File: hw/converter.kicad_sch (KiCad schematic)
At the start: 16 parts, among them J301 1935776, J302 1935776, Q301 SW_L, Q302 SW_H

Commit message: hw changes
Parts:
- HS301: footprint mppt:WayinTop_HS -> footprints:WayinTop_HS
- J301, J302: footprint mppt:1935776 -> footprints:1935776
- L301: footprint mppt:B65878E1012D001 -> footprints:B65878E1012D001
- Q301, Q302: footprint mppt:EPC2307 -> footprints:EPC2307
- TP302, TP410: footprint mppt:SignalTP -> footprints:SignalTP
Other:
- moved on the sheet: C304
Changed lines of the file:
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@@
   (junction (at 134.62 71.12) (diameter 0) (color 0 0 0 0)
   )
-  (junction (at 198.755 71.12) (diameter 0) (color 0 0 0 0)
+  (junction (at 198.12 71.12) (diameter 0) (color 0 0 0 0)
   )
   (junction (at 157.48 85.09) (diameter 0) (color 0 0 0 0)
@@
   (junction (at 180.34 109.22) (diameter 0) (color 0 0 0 0)
   )
-  (junction (at 198.755 109.22) (diameter 0) (color 0 0 0 0)
+  (junction (at 198.12 109.22) (diameter 0) (color 0 0 0 0)
   )
   (junction (at 156.21 109.22) (diameter 0) (color 0 0 0 0)
@@
     (stroke (width 0) (type default))
   )
-  (wire (pts (xy 180.34 71.12) (xy 198.755 71.12))
+  (wire (pts (xy 180.34 71.12) (xy 198.12 71.12))
     (stroke (width 0) (type default))
   )
@@
     (stroke (width 0) (type default))
   )
-  (wire (pts (xy 198.755 93.98) (xy 198.755 109.22))
+  (wire (pts (xy 198.12 93.98) (xy 198.12 109.22))
     (stroke (width 0) (type default))
   )
@@
     (stroke (width 0) (type default))
   )
-  (wire (pts (xy 198.755 71.12) (xy 214.63 71.12))
+  (wire (pts (xy 198.12 71.12) (xy 214.63 71.12))
     (stroke (width 0) (type default))
   )
@@
     (stroke (width 0) (type default))
   )
-  (wire (pts (xy 180.34 109.22) (xy 198.755 109.22))
+  (wire (pts (xy 180.34 109.22) (xy 198.12 109.22))
     (stroke (width 0) (type default))
   )
@@
     (stroke (width 0) (type default))
   )
-  (wire (pts (xy 198.755 71.12) (xy 198.755 86.36))
+  (wire (pts (xy 198.12 71.12) (xy 198.12 86.36))
     (stroke (width 0) (type default))
   )
@@
     (stroke (width 0) (type default))
   )
-  (wire (pts (xy 198.755 109.22) (xy 214.63 109.22))
+  (wire (pts (xy 198.12 109.22) (xy 214.63 109.22))
     (stroke (width 0) (type default))
   )
@@
       (effects (font (size 1 1)))
     )
-    (property "Footprint" "mppt:1935776" (at 40.64 88.9 0)
+    (property "Footprint" "footprints:1935776" (at 40.64 88.9 0)
       (effects (font (size 1.27 1.27)) (justify bottom) hide)
     )
@@
       (effects (font (size 1 1)) (justify left))
     )
-    (property "Footprint" "mppt:EPC2307" (at 160.02 87.63 0)
+    (property "Footprint" "footprints:EPC2307" (at 160.02 87.63 0)
       (effects (font (size 1.27 1.27)) hide)
     )
@@
       (effects (font (size 1 1)))
     )
-    (property "Footprint" "mppt:1935776" (at 256.54 88.9 0)
+    (property "Footprint" "footprints:1935776" (at 256.54 88.9 0)
       (effects (font (size 1.27 1.27)) (justify bottom) hide)
     )
@@
       (effects (font (size 1 1)))
     )
-    (property "Footprint" "mppt:EPC2307" (at 167.64 73.66 0)
+    (property "Footprint" "footprints:EPC2307" (at 167.64 73.66 0)
       (effects (font (size 1.27 1.27)) hide)
     )
@@
       (effects (font (size 1 1)) (justify left))
     )
-    (property "Footprint" "mppt:SignalTP" (at 114.3 97.79 0)
+    (property "Footprint" "footprints:SignalTP" (at 114.3 97.79 0)
       (effects (font (size 1.27 1.27)) hide)
     )
@@
       (effects (font (size 1 1)) (justify left))
     )
-    (property "Footprint" "mppt:SignalTP" (at 165.1 90.17 0)
+    (property "Footprint" "footprints:SignalTP" (at 165.1 90.17 0)
       (effects (font (size 1.27 1.27)) hide)
     )
@@
       (effects (font (size 1 1)) (justify left))
     )
-    (property "Footprint" "mppt:WayinTop_HS" (at 159.0548 55.88 0)
+    (property "Footprint" "footprints:WayinTop_HS" (at 159.0548 55.88 0)
       (effects (font (size 1.27 1.27)) hide)
     )
@@
     )
   )
-  (symbol (lib_id "Device:C") (at 198.755 90.17 0) (unit 1)
-    (in_bom yes) (on_board yes) (dnp no)
-    (property "Reference" "C304" (at 202.565 88.8999 0)
-      (effects (font (size 1 1)) (justify left))
-    )
-    (property "Value" "18uF" (at 202.565 91.4399 0)
-      (effects (font (size 1 1)) (justify left))
-    )
-    (property "Footprint" "Capacitor_THT:C_Radial_D10.0mm_H16.0mm_P5.00mm" (at 199.7202 93.98 0)
-      (effects (font (size 1.27 1.27)) hide)
-    )
-    (property "Datasheet" "https://www.mouser.com/datasheet/2/212/KEM_A4072_A759-1104329.pdf" (at 198.755 90.17 0)
-      (effects (font (size 1.27 1.27)) hide)
-    )
-    (property "Distributor" "Mouser" (at 198.755 90.17 0)
-      (effects (font (size 1.27 1.27)) hide)
-    )
-    (property "Manufacturer" "KEMET" (at 198.755 90.17 0)
-      (effects (font (size 1.27 1.27)) hide)
-    )
-    (property "P/N" "80-A759MS186M2CAAE90" (at 198.755 90.17 0)
-      (effects (font (size 1.27 1.27)) hide)
-    )
-    (property "LCSC Part #" "" (at 198.755 90.17 0)
-      (effects (font (size 1.27 1.27)) hide)
-    )
-    (property "Cost" "2.58" (at 198.755 90.17 0)
+  (symbol (lib_id "Device:C") (at 198.12 90.17 0) (unit 1)
+    (in_bom yes) (on_board yes) (dnp no)
+    (property "Reference" "C304" (at 201.93 88.8999 0)
+      (effects (font (size 1 1)) (justify left))
+    )
+    (property "Value" "18uF" (at 201.93 91.4399 0)
+      (effects (font (size 1 1)) (justify left))
+    )
+    (property "Footprint" "Capacitor_THT:C_Radial_D10.0mm_H16.0mm_P5.00mm" (at 199.0852 93.98 0)
+      (effects (font (size 1.27 1.27)) hide)
+    )
+    (property "Datasheet" "https://www.mouser.com/datasheet/2/212/KEM_A4072_A759-1104329.pdf" (at 198.12 90.17 0)
+      (effects (font (size 1.27 1.27)) hide)
+    )
+    (property "Distributor" "Mouser" (at 198.12 90.17 0)
+      (effects (font (size 1.27 1.27)) hide)
+    )
+    (property "Manufacturer" "KEMET" (at 198.12 90.17 0)
+      (effects (font (size 1.27 1.27)) hide)
+    )
+    (property "P/N" "80-A759MS186M2CAAE90" (at 198.12 90.17 0)
+      (effects (font (size 1.27 1.27)) hide)
+    )
+    (property "LCSC Part #" "" (at 198.12 90.17 0)
+      (effects (font (size 1.27 1.27)) hide)
+    )
+    (property "Cost" "2.58" (at 198.12 90.17 0)
       (effects (font (size 1.27 1.27)) hide)
     )
@@
       (effects (font (size 1 1)))
     )
-    (property "Footprint" "mppt:B65878E1012D001" (at 101.6 50.8 0)
+    (property "Footprint" "footprints:B65878E1012D001" (at 101.6 50.8 0)
       (effects (font (size 1.27 1.27)) (justify left) hide)
     )

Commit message: v0.2.0
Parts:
- removed C302: CP, TestPoint:TestPoint_2Pads_Pitch2.54mm_Drill0.8mm, symbol Device:C
- removed D301: Schottky, TestPoint:TestPoint_2Pads_Pitch2.54mm_Drill0.8mm, symbol Device:D_Schottky
- removed D302: D_TVS, Diode_SMD:D_SMC, symbol Device:D_TVS
- removed HS301: Heatsink_Pad, footprints:WayinTop_HS, symbol Mechanical:Heatsink
- removed J301, J302: 1935776, footprints:1935776, symbol 1935776:1935776
- removed L301: B65878E1012D001, footprints:B65878E1012D001, symbol B65878E1012D001:B65878E1012D001
- removed R301: R, TestPoint:TestPoint_2Pads_Pitch2.54mm_Drill0.8mm, symbol Device:R
- removed TP410: TestPoint_2Pole, footprints:SignalTP, symbol Connector:TestPoint_2Pole
- added C301: 2.2uF, Capacitor_SMD:C_2220_5650Metric, symbol Device:C
- added F301, F302: Fuse_Small, footprints:littelfuse_05200101Z, symbol Device:Fuse
- added J301, J302: XT60PW-M, Connector_AMASS:AMASS_XT60PW-M_1x02_P7.20mm_Horizontal, symbol amass_XT60PW_M:XT60PW-M
- added L301: B65878E1012D001, footprints:tdk_B65878E1012D001, symbol tdk_B65878E1012D001:B65878E1012D001
- Q301, Q302: footprint footprints:EPC2307 -> footprints:epc_EPC2307
- TP301: renamed from TP302; value TestPoint_2Pole -> VSW_TP; footprint footprints:SignalTP -> TestPoint:TestPoint_2Pads_Pitch5.08mm_Drill1.3mm
- renumbered C301 to C302
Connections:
- net GND: now also C301.2
- net V_ARR+: now also C301.1, F301.2, L301.A
- net V_ARR-: now also J301.2
- net V_BATT+: now also F302.1
- net V_BATT-: now also J302.2
- net V_SW: now also L301.B
- new net: F301.1, J301.1
- new net: F302.2, J302.1
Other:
- note added: "Converter"
- company: UT LHR Solar -> LHR Solar
- moved on the sheet: C302, C303, Q301, Q302, TP301

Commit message: bugfix for wrong adc pin for batt current measurements
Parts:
- Q301: value SW_L -> EPC2307
- Q302: value SW_H -> EPC2307
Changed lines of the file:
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@@
       (effects (font (size 1 1)) (justify left))
     )
-    (property "Value" "SW_L" (at 129.54 102.87 0)
+    (property "Value" "EPC2307" (at 129.54 102.87 0)
       (effects (font (size 1 1)) (justify left))
     )
@@
       (effects (font (size 1 1)))
     )
-    (property "Value" "SW_H" (at 154.94 85.09 90)
+    (property "Value" "EPC2307" (at 156.21 85.09 90)
       (effects (font (size 1 1)))
     )
@@
       (effects (font (size 1 1)) hide)
     )
-    (property "Datasheet" "~" (at 144.78 106.68 0)
-      (effects (font (size 1 1)) hide)
-    )
+    (property "Datasheet" "" (at 144.78 106.68 0)
+      (effects (font (size 1 1)) hide)
+    )

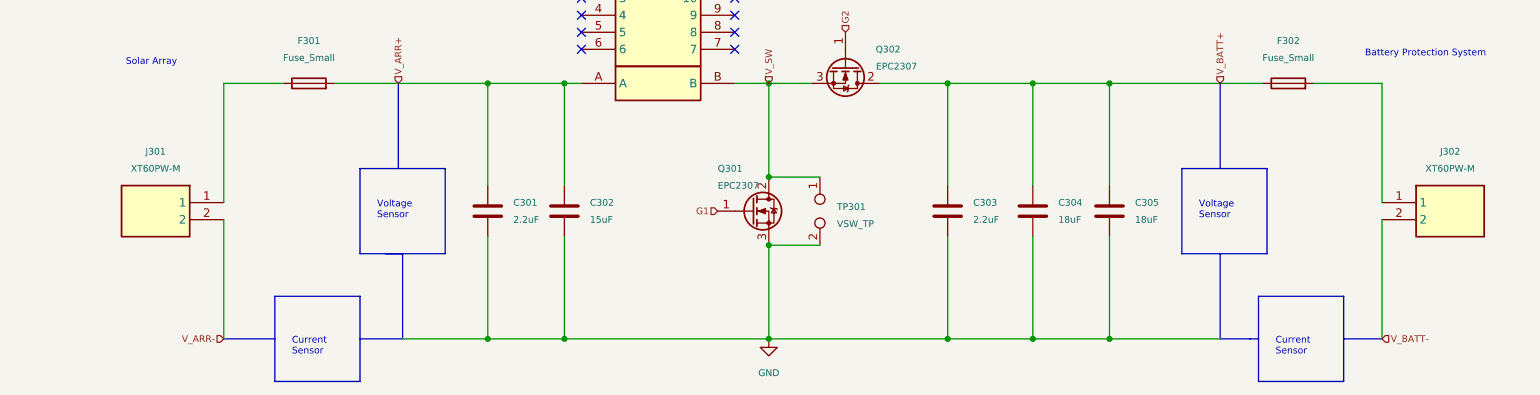
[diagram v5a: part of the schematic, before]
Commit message: fix for swapped xt60 connectors
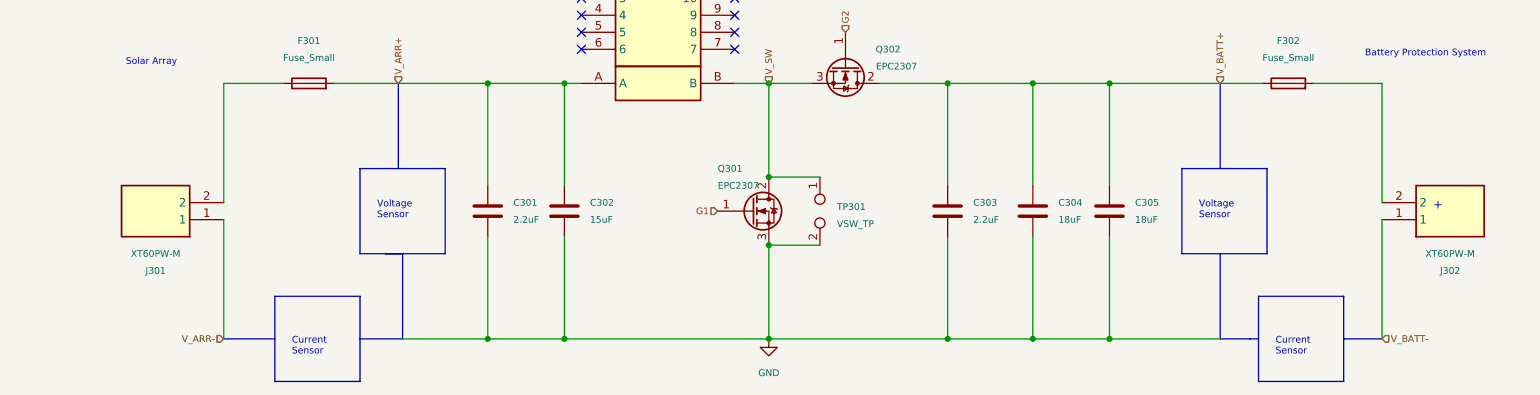
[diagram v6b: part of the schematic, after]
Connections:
- net V_ARR-: now also J301.1; no longer J301.2
- net V_BATT-: now also J302.1; no longer J302.2
- net at F301.1: now also J301.2; no longer J301.1
- net at F302.2: now also J302.2; no longer J302.1
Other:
- note added: "+"
- moved on the sheet: J301
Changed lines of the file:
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@@
+    (stroke (width 0) (type default))
+  )
+  (wire (pts (xy 55.88 105.41) (xy 55.88 87.63))
     (stroke (width 0) (type default))
   )
@@
   )
   (polyline (pts (xy 198.755 100.33) (xy 211.455 100.33))
-    (stroke (width 0) (type default))
-  )
-  (wire (pts (xy 55.88 105.41) (xy 55.88 87.63))
     (stroke (width 0) (type default))
   )
@@
   (text "Voltage\nSensor" (at 201.295 107.95 0)
     (effects (font (size 1 1)) (justify left bottom))
+  )
+  (text "+" (at 236.22 106.68 0)
+    (effects (font (size 1.27 1.27)) (justify left bottom))
   )
   (text "Current\nSensor" (at 66.04 128.27 0)
@@
     )
   )
-  (symbol (lib_id "amass_XT60PW_M:XT60PW-M") (at 55.88 105.41 0) (mirror y) (unit 1)
-    (in_bom yes) (on_board yes) (dnp no)
-    (property "Reference" "J301" (at 45.72 97.79 0)
-      (effects (font (size 1 1)))
-    )
-    (property "Value" "XT60PW-M" (at 45.72 100.33 0)
-      (effects (font (size 1 1)))
-    )
-    (property "Footprint" "Connector_AMASS:AMASS_XT60PW-M_1x02_P7.20mm_Horizontal" (at 39.37 200.33 0)
+  (symbol (lib_id "amass_XT60PW_M:XT60PW-M") (at 55.88 107.95 180) (unit 1)
+    (in_bom yes) (on_board yes) (dnp no)
+    (property "Reference" "J301" (at 45.72 115.57 0)
+      (effects (font (size 1 1)))
+    )
+    (property "Value" "XT60PW-M" (at 45.72 113.03 0)
+      (effects (font (size 1 1)))
+    )
+    (property "Footprint" "Connector_AMASS:AMASS_XT60PW-M_1x02_P7.20mm_Horizontal" (at 39.37 13.03 0)
       (effects (font (size 1 1)) (justify left top) hide)
     )
-    (property "Datasheet" "https://www.tme.eu/Document/9b8d0c5eb7094295f3d3112c214d3ade/XT60PW%20SPEC.pdf" (at 39.37 300.33 0)
+    (property "Datasheet" "https://www.tme.eu/Document/9b8d0c5eb7094295f3d3112c214d3ade/XT60PW%20SPEC.pdf" (at 39.37 -86.97 0)
       (effects (font (size 1 1)) (justify left top) hide)
     )
-    (property "Distributor" "JLCPCB" (at 55.88 105.41 0)
-      (effects (font (size 1 1)) hide)
-    )
-    (property "Manufacturer" "AMASS" (at 55.88 105.41 0)
-      (effects (font (size 1 1)) hide)
-    )
-    (property "P/N" "XT60PW-M" (at 55.88 105.41 0)
-      (effects (font (size 1 1)) hide)
-    )
-    (property "LCSC Part #" "C98732" (at 55.88 105.41 0)
-      (effects (font (size 1 1)) hide)
-    )
-    (property "Cost" "0.3845" (at 55.88 105.41 0)
-      (effects (font (size 1 1)) hide)
-    )
-    (property "Notes" "Also available from TME." (at 55.88 105.41 0)
+    (property "Distributor" "JLCPCB" (at 55.88 107.95 0)
+      (effects (font (size 1 1)) hide)
+    )
+    (property "Manufacturer" "AMASS" (at 55.88 107.95 0)
+      (effects (font (size 1 1)) hide)
+    )
+    (property "P/N" "XT60PW-M" (at 55.88 107.95 0)
+      (effects (font (size 1 1)) hide)
+    )
+    (property "LCSC Part #" "C98732" (at 55.88 107.95 0)
+      (effects (font (size 1 1)) hide)
+    )
+    (property "Cost" "0.3845" (at 55.88 107.95 0)
+      (effects (font (size 1 1)) hide)
+    )
+    (property "Notes" "Also available from TME." (at 55.88 107.95 0)
       (effects (font (size 1 1)) hide)
     )
@@
     )
   )
-  (symbol (lib_name "XT60PW-M_1") (lib_id "amass_XT60PW_M:XT60PW-M") (at 228.6 105.41 0) (unit 1)
-    (in_bom yes) (on_board yes) (dnp no)
-    (property "Reference" "J302" (at 238.76 97.79 0)
-      (effects (font (size 1 1)))
-    )
-    (property "Value" "XT60PW-M" (at 238.76 100.33 0)
-      (effects (font (size 1 1)))
-    )
-    (property "Footprint" "Connector_AMASS:AMASS_XT60PW-M_1x02_P7.20mm_Horizontal" (at 245.11 200.33 0)
+  (symbol (lib_name "XT60PW-M_1") (lib_id "amass_XT60PW_M:XT60PW-M") (at 228.6 107.95 0) (mirror x) (unit 1)
+    (in_bom yes) (on_board yes) (dnp no)
+    (property "Reference" "J302" (at 238.76 115.57 0)
+      (effects (font (size 1 1)))
+    )
+    (property "Value" "XT60PW-M" (at 238.76 113.03 0)
+      (effects (font (size 1 1)))
+    )
+    (property "Footprint" "Connector_AMASS:AMASS_XT60PW-M_1x02_P7.20mm_Horizontal" (at 245.11 13.03 0)
       (effects (font (size 1 1)) (justify left top) hide)
     )
-    (property "Datasheet" "https://www.tme.eu/Document/9b8d0c5eb7094295f3d3112c214d3ade/XT60PW%20SPEC.pdf" (at 245.11 300.33 0)
+    (property "Datasheet" "https://www.tme.eu/Document/9b8d0c5eb7094295f3d3112c214d3ade/XT60PW%20SPEC.pdf" (at 245.11 -86.97 0)
       (effects (font (size 1 1)) (justify left top) hide)
     )
-    (property "Distributor" "JLCPCB" (at 228.6 105.41 0)
-      (effects (font (size 1 1)) hide)
-    )
-    (property "Manufacturer" "AMASS" (at 228.6 105.41 0)
-      (effects (font (size 1 1)) hide)
-    )
-    (property "P/N" "XT60PW-M" (at 228.6 105.41 0)
-      (effects (font (size 1 1)) hide)
-    )
-    (property "LCSC Part #" "C98732" (at 228.6 105.41 0)
-      (effects (font (size 1 1)) hide)
-    )
-    (property "Cost" "0.3845" (at 228.6 105.41 0)
-      (effects (font (size 1 1)) hide)
-    )
-    (property "Notes" "Also available from TME." (at 228.6 105.41 0)
-      (effects (font (size 1 1)) hide)
-    )
+    (property "Distributor" "JLCPCB" (at 228.6 107.95 0)
+      (effects (font (size 1 1)) hide)
+    )
+    (property "Manufacturer" "AMASS" (at 228.6 107.95 0)
+      (effects (font (size 1 1)) hide)
+    )
+    (property "P/N" "XT60PW-M" (at 228.6 107.95 0)
+      (effects (font (size 1 1)) hide)
+    )
+    (property "LCSC Part #" "C98732" (at 228.6 107.95 0)
+      (effects (font (size 1 1)) hide)
+    )
+    (property "Cost" "0.3845" (at 228.6 107.95 0)
+      (effects (font (size 1 1)) hide)
+    )
+    (property "Notes" "Also available from TME." (at 228.6 107.95 0)
+      (effects (font (size 1 1)) hide)
+    )

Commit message: init sch changes
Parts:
- added D3: 160V, symbol Device:D_Zener
- added R3: 330, symbol Device:R
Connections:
- net V_ARR- is gone; now on net GND: J301.1
- net V_BATT- is gone; now on net GND: J302.1
- net GND: now also R3.2
- net G1 renamed SWL
- net G2 renamed SWH
- net V_ARR+ renamed V_{DCI+}
- net V_{DCI+}: no longer F301.2
- net V_BATT+ renamed V_{DCO+}
- net V_{DCO+}: no longer F302.1
- net V_SW renamed V_{SW}
- net V_{SW}: now also D3.1 (K)
- new net: D3.2 (A), R3.1
- new net V_{ARR+}: F301.2
- new net V_{BATT+}: F302.1
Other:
- note added: "0.5A"
- note added: "Protect against load dump surge; Not a snubber circuit"
- note removed: "Current Sensor"
- note removed: "Voltage Sensor"
- moved on the sheet: C301, C302, C303, C304, C305, F301, F302, J301, J302, L301, Q301, Q302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

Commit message: v0.3.0rc (v1.0.0rc) sch complete
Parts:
- removed C301, C303: 2.2uF, Capacitor_SMD:C_2220_5650Metric, symbol Device:C
- removed C302: 15uF, Capacitor_THT:C_Radial_D8.0mm_H11.5mm_P3.50mm, symbol Device:C
- removed C304, C305: 18uF, Capacitor_THT:C_Radial_D10.0mm_H16.0mm_P5.00mm, symbol Device:C
- removed D3: 160V, symbol Device:D_Zener
- removed F301, F302: Fuse_Small, footprints:littelfuse_05200101Z, symbol Device:Fuse
- removed L301: B65878E1012D001, footprints:tdk_B65878E1012D001, symbol tdk_B65878E1012D001:B65878E1012D001
- removed Q301, Q302: EPC2307, footprints:epc_EPC2307, symbol Device:Q_NMOS_GDS
- removed R3: 330, symbol Device:R
- removed TP301: VSW_TP, TestPoint:TestPoint_2Pads_Pitch5.08mm_Drill1.3mm, symbol Connector:TestPoint_2Pole
- added C301, C303: 2.2u, Capacitor_SMD:C_2220_5750Metric_Pad1.97x5.40mm_HandSolder, symbol Device:C_Small
- added C302, C304, C305: 18u, Capacitor_THT:C_Radial_D10.0mm_H16.0mm_P5.00mm, symbol Device:C_Polarized
- added D301, D303: 150, Diode_SMD:D_SMA, symbol Device:D_Zener
- added D302: 150, Diode_SMD:D_SMA, symbol Diode:SMAJ150CA
- added L301: PQ26/25, footprints:ferroxcube_CSV-PQ26_25-1S-12P-ZF, symbol ferroxcube_CSV-PQ26_25-1S-12P-ZF:CSV-PQ26/25-1S-12P-ZF
- added Q301, Q302: EPC2059, footprints:epc_EPC2059, symbol epc_EPC2059:EPC2059
- J301, J302: footprint Connector_AMASS:AMASS_XT60PW-M_1x02_P7.20mm_Horizontal -> footprints:amass_XT60PW_M; Cost 0.3845 -> 1.080; Distributor JLCPCB -> TME; Notes Also available from TME. -> (none)
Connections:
- net V_{ARR+}: now also J301.2
- net V_{DCI+}: now also C301.1, C302.1, D301.1 (K), L301.A
- net V_{DCO+}: now also C303.1, C304.1, C305.1, D303.1 (K), Q302.3 (D), Q302.5 (D)
- net V_{SW}: now also D302.2 (A2), L301.B, Q301.3 (D), Q301.5 (D), Q302.2 (S), Q302.4 (S), Q302.6 (S)
- net V_{BAT+}: now reaches J302.2
- net GND renamed V_{ARR-}
- net V_{ARR-}: no longer J302.1
- new net: L301.1 (x), L301.2 (x), L301.3 (x), L301.4 (x), L301.5 (x), L301.6 (x)
- new net: L301.10 (x), L301.11 (x), L301.12 (x), L301.7 (x), L301.8 (x), L301.9 (x)
- new net GNDPWR: C301.2, C302.2, C303.2, C304.2, C305.2, D301.2 (A), D302.1 (A1), D303.2 (A), Q301.2 (S), Q301.4 (S), Q301.6 (S)
- new net SWHO: Q302.1 (G)
- new net SWLO: Q301.1 (G)
- new net V_{BAT-}: J302.1
- no-connect marks 12 -> 0
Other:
- note added: "Measure voltage in front of load"
- note added: "Power Ground Reference"
- note added: "Switch Node"
- note added: "Switch node surge protection in particular failure modes, not meant to be a snubber."
- note removed: "+"
- note removed: "0.5A"
- note removed: "Battery Protection System"
- note removed: "Protect against load dump surge; Not a snubber circuit"
- note removed: "Solar Array"
